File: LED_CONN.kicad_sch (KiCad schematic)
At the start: 4 parts, among them U3 SM02B-SRSS-TB-LF-SN, U4 SM02B-SRSS-TB-LF-SN

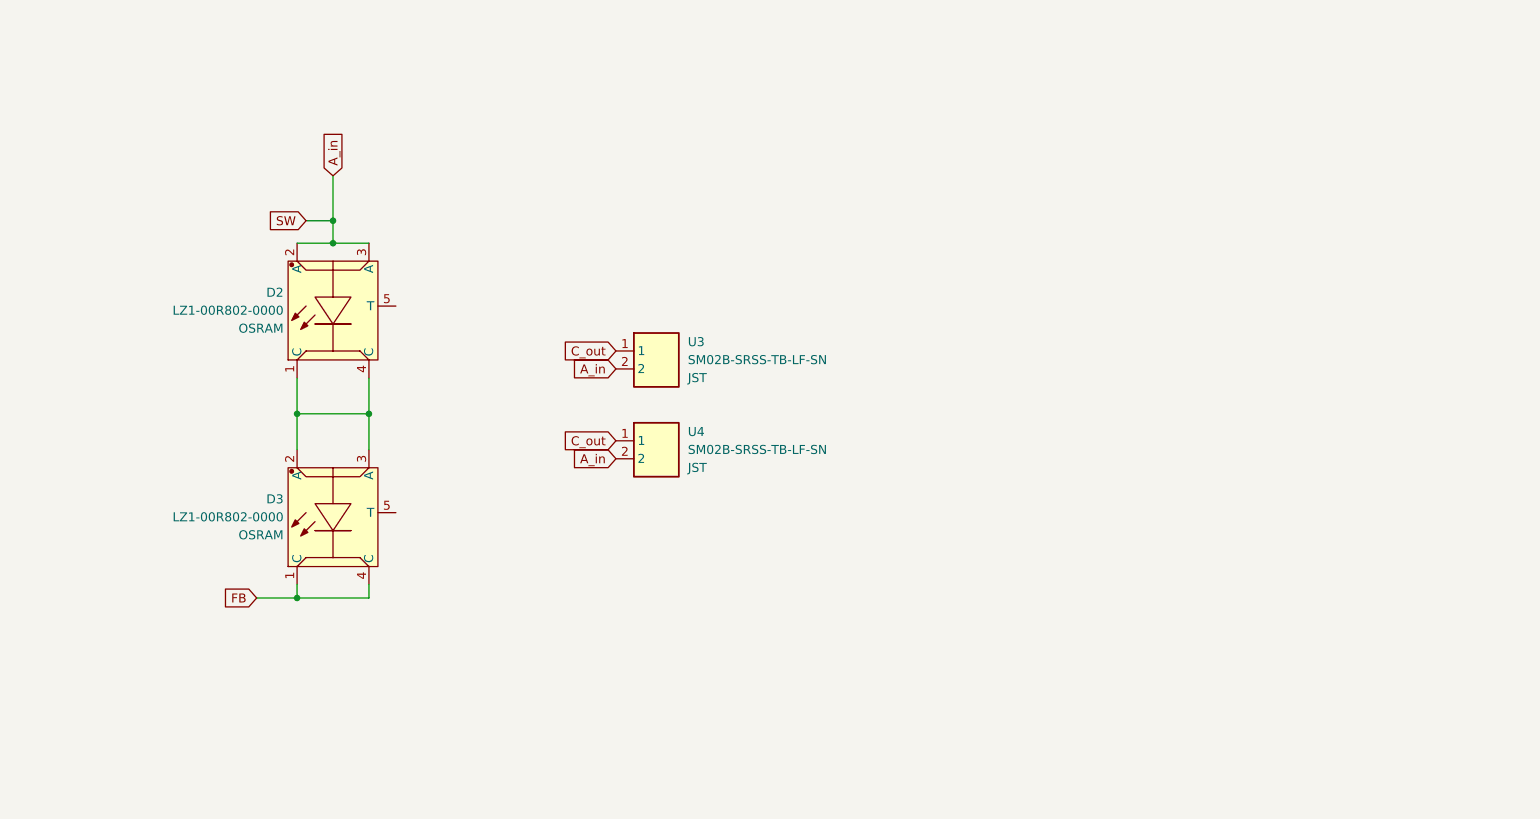
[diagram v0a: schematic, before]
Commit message: Change pinout of B2B connectors
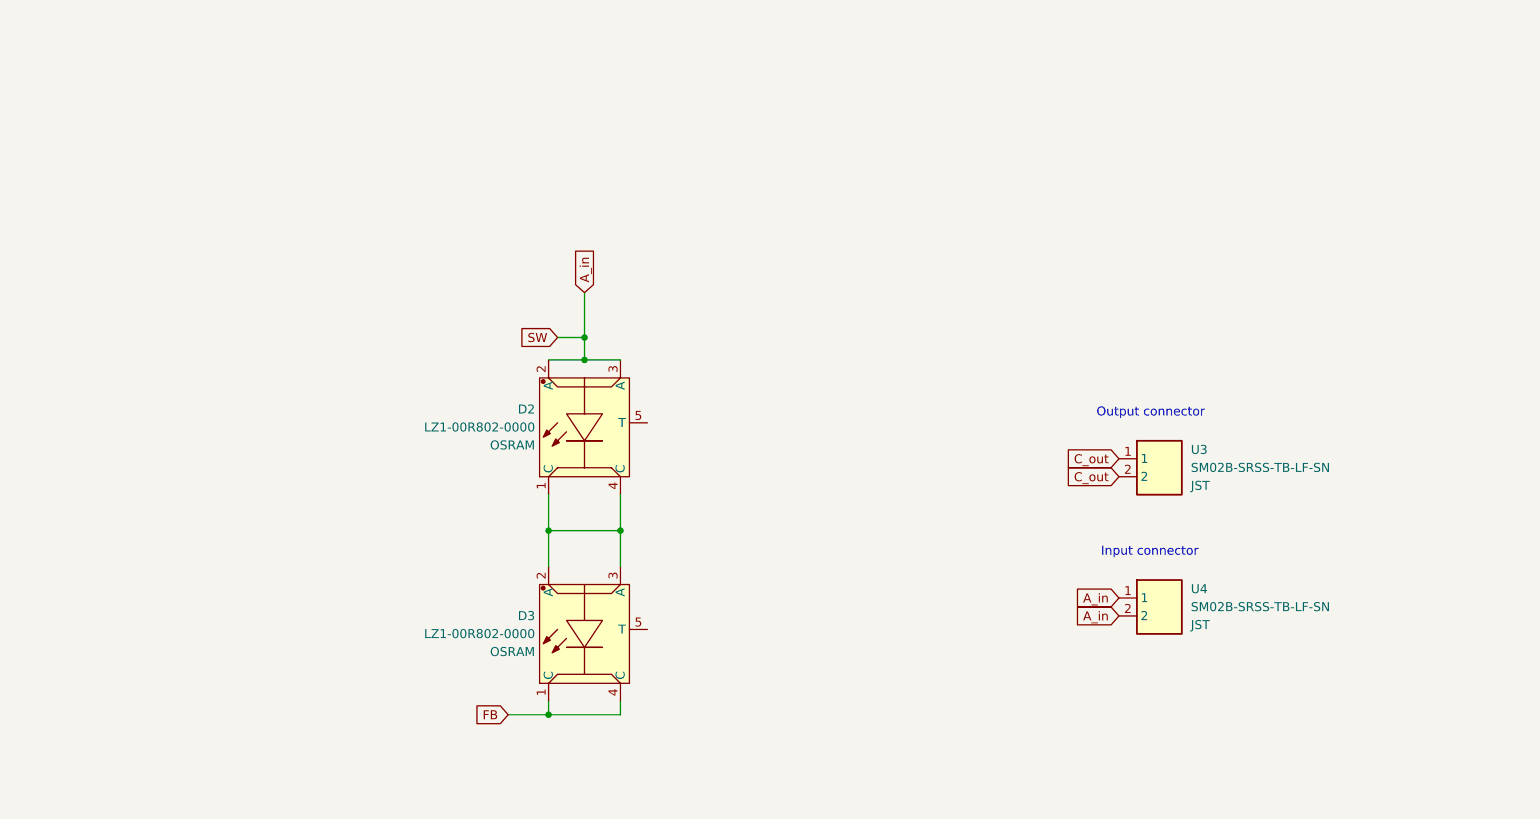
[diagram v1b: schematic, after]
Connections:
- net A_in: now also U4.1; no longer U3.2
- net C_out: now also U3.2; no longer U4.1
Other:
- note added: "Input connector"
- note added: "Output connector"
- moved on the sheet: D2, D3, U3, U4

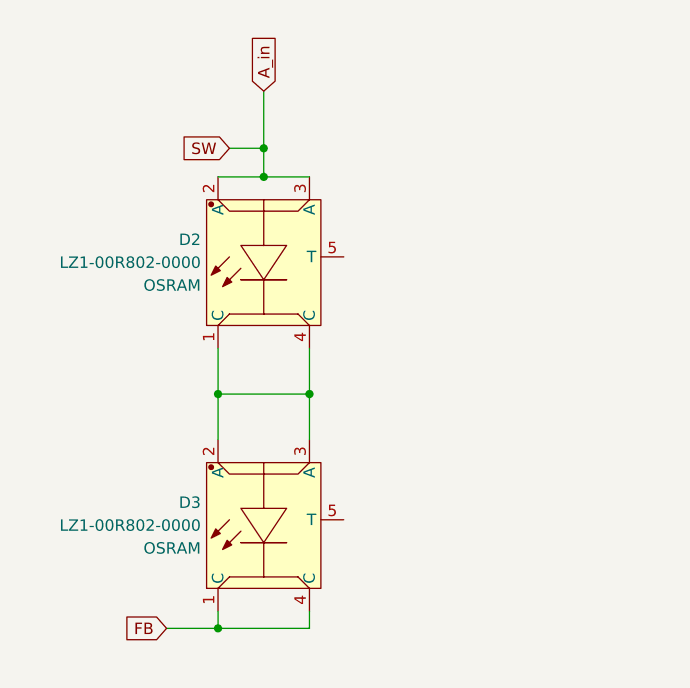
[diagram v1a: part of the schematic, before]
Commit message: Add thermal pad label
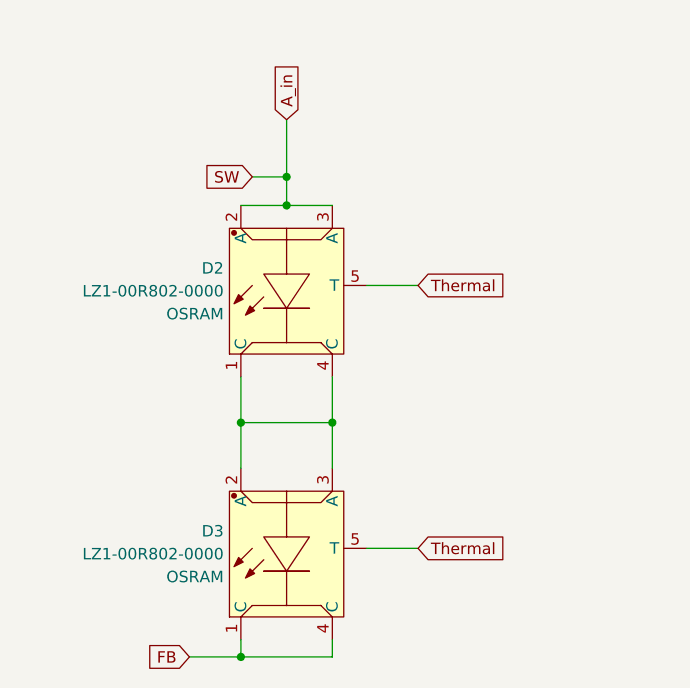
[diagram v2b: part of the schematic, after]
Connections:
- net Thermal: now reaches D3.5 (T)
- net Thermal: now also D2.5 (T)
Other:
- moved on the sheet: D2, D3

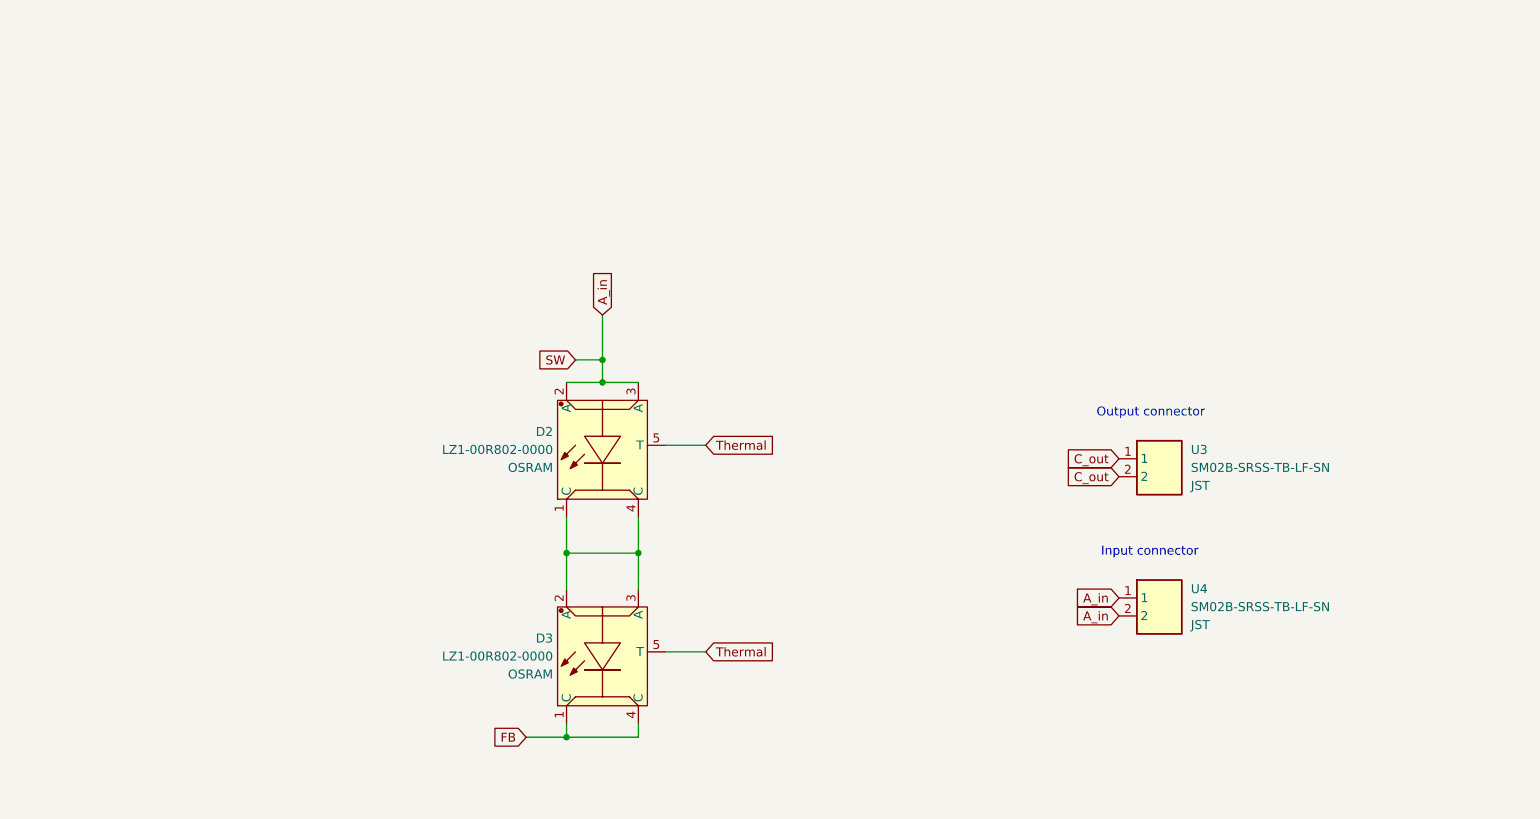
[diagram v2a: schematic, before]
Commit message: Change diodes power rail labels
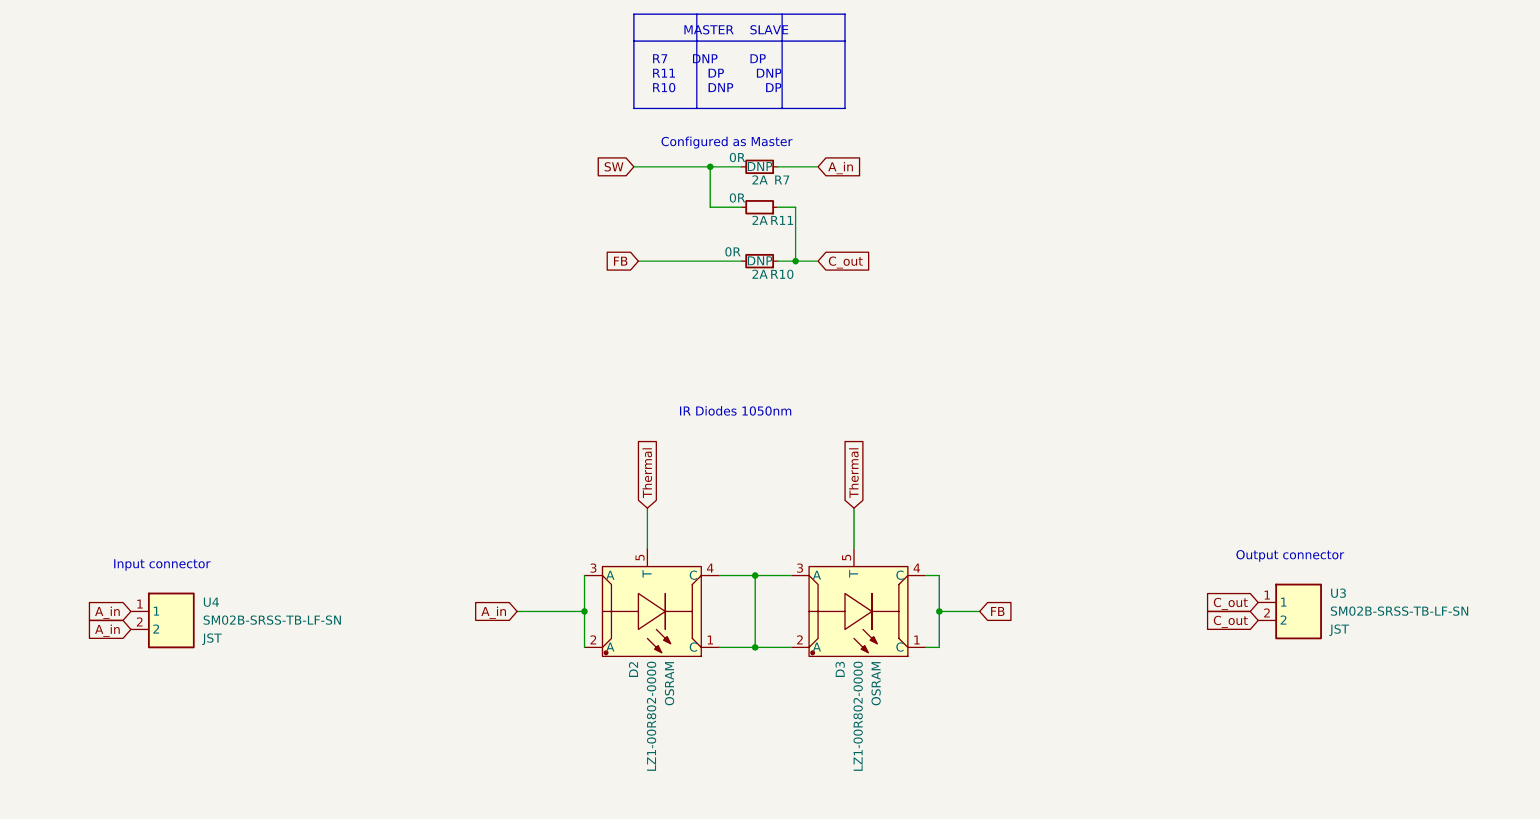
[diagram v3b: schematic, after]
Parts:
- added R10, R11, R7: R_0R_1206, antmicro-footprints:R_1206_3216Metric, symbol antmicroResistorsmisc:R_0R_1206
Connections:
- net A_in: now also R7.1
- net C_out: now also R10.1, R11.1
- net FB: now also R10.2
- new net SW: R11.2, R7.2
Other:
- note added: "Configured as Master"
- note added: "IR Diodes 1050nm"
- note added: "MASTER SLAVE R7 DNP DP R11 DP DNP R10 DNP DP"
- moved on the sheet: D2, D3, U3, U4
